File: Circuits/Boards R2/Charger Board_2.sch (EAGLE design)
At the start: 70 parts, among them CON1 ISP(2X3), CON10 HEADER_3X1, CON11 HEADER_3X1, CON12 HEADER_3X1, CON13 HEADER_4X1, CON2 SCREWTERMINAL_1X2, CON3 HEADER_3X1, CON4 HEADER_3X1, CON5 HEADER_3X1, CON6 HEADER_3X1, CON7 HEADER_3X1, CON8 HEADER_3X1, CON9 HEADER_3X1, IC1 NCP1117DT33G, T1 NPN2N2222, T2 NPN2N2222, T3 SI4421DY, U1 ATMEGA324P, U2 ACS711

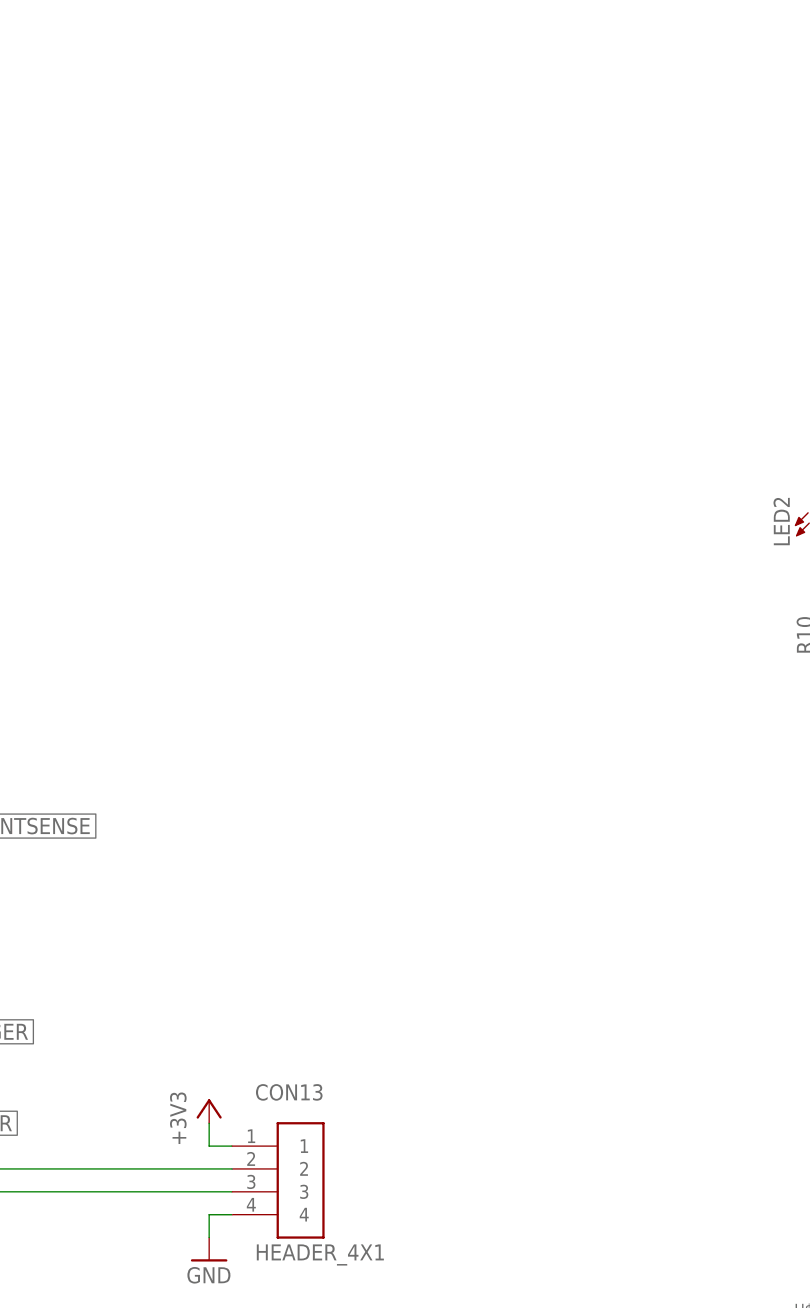
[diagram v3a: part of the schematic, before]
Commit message: 
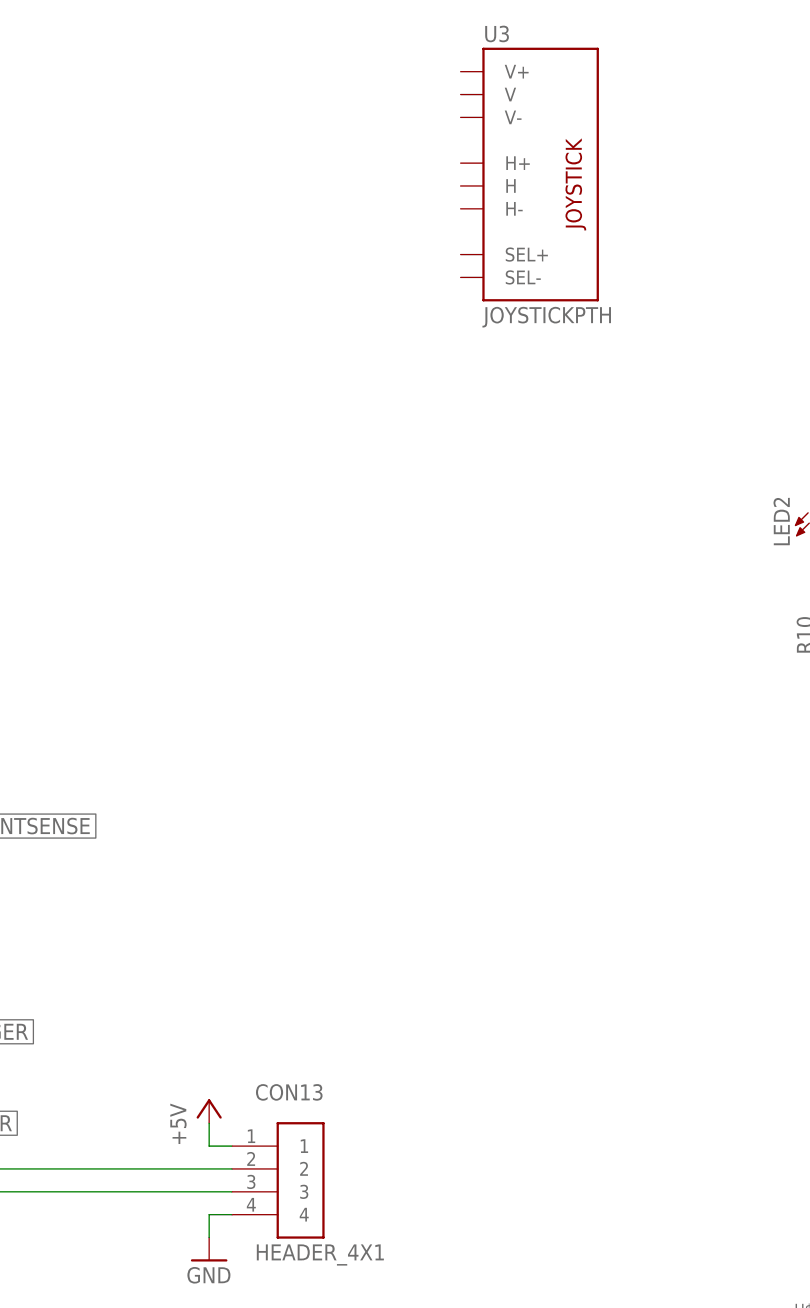
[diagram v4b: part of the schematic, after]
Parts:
- added U3: JOYSTICKPTH, SparkFun:JOYSTICKPTH
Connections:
- net +3V3: no longer CON13.1
- net +5V: now also CON13.1
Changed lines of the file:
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@@
 <layer number="51" name="tDocu" color="6" fill="1" visible="no" active="no"/>
 <layer number="52" name="bDocu" color="7" fill="1" visible="no" active="no"/>
+<layer number="53" name="tGND_GNDA" color="7" fill="9" visible="no" active="no"/>
+<layer number="54" name="bGND_GNDA" color="1" fill="9" visible="no" active="no"/>
+<layer number="56" name="wert" color="7" fill="1" visible="no" active="no"/>
 <layer number="91" name="Nets" color="2" fill="1" visible="yes" active="yes"/>
 <layer number="92" name="Busses" color="1" fill="1" visible="yes" active="yes"/>
@@
 <layer number="97" name="Info" color="7" fill="1" visible="yes" active="yes"/>
 <layer number="98" name="Guide" color="6" fill="1" visible="yes" active="yes"/>
+<layer number="100" name="Muster" color="7" fill="1" visible="no" active="no"/>
+<layer number="101" name="Patch_Top" color="12" fill="4" visible="no" active="yes"/>
+<layer number="102" name="Vscore" color="7" fill="1" visible="no" active="yes"/>
+<layer number="103" name="tMap" color="7" fill="1" visible="no" active="yes"/>
+<layer number="104" name="Name" color="16" fill="1" visible="no" active="yes"/>
+<layer number="105" name="tPlate" color="7" fill="1" visible="no" active="yes"/>
+<layer number="106" name="bPlate" color="7" fill="1" visible="no" active="yes"/>
+<layer number="107" name="Crop" color="7" fill="1" visible="no" active="yes"/>
+<layer number="116" name="Patch_BOT" color="9" fill="4" visible="no" active="yes"/>
+<layer number="121" name="_tsilk" color="7" fill="1" visible="no" active="yes"/>
+<layer number="122" name="_bsilk" color="7" fill="1" visible="no" active="yes"/>
+<layer number="125" name="_tNames" color="7" fill="1" visible="no" active="yes"/>
+<layer number="144" name="Drill_legend" color="7" fill="1" visible="no" active="yes"/>
+<layer number="151" name="HeatSink" color="7" fill="1" visible="no" active="yes"/>
 <layer number="200" name="200bmp" color="1" fill="10" visible="no" active="no"/>
+<layer number="201" name="201bmp" color="2" fill="10" visible="no" active="yes"/>
+<layer number="202" name="202bmp" color="3" fill="10" visible="no" active="yes"/>
+<layer number="203" name="203bmp" color="4" fill="10" visible="no" active="yes"/>
+<layer number="204" name="204bmp" color="5" fill="10" visible="no" active="yes"/>
+<layer number="205" name="205bmp" color="6" fill="10" visible="no" active="yes"/>
+<layer number="206" name="206bmp" color="7" fill="10" visible="no" active="yes"/>
+<layer number="207" name="207bmp" color="8" fill="10" visible="no" active="yes"/>
+<layer number="208" name="208bmp" color="9" fill="10" visible="no" active="yes"/>
+<layer number="209" name="209bmp" color="7" fill="1" visible="no" active="yes"/>
+<layer number="210" name="210bmp" color="7" fill="1" visible="no" active="yes"/>
+<layer number="211" name="211bmp" color="7" fill="1" visible="no" active="yes"/>
+<layer number="212" name="212bmp" color="7" fill="1" visible="no" active="yes"/>
+<layer number="213" name="213bmp" color="7" fill="1" visible="no" active="yes"/>
+<layer number="214" name="214bmp" color="7" fill="1" visible="no" active="yes"/>
+<layer number="215" name="215bmp" color="7" fill="1" visible="no" active="yes"/>
+<layer number="216" name="216bmp" color="7" fill="1" visible="no" active="yes"/>
+<layer number="217" name="217bmp" color="18" fill="1" visible="no" active="no"/>
+<layer number="218" name="218bmp" color="19" fill="1" visible="no" active="no"/>
+<layer number="219" name="219bmp" color="20" fill="1" visible="no" active="no"/>
+<layer number="220" name="220bmp" color="21" fill="1" visible="no" active="no"/>
+<layer number="221" name="221bmp" color="22" fill="1" visible="no" active="no"/>
+<layer number="222" name="222bmp" color="23" fill="1" visible="no" active="no"/>
+<layer number="223" name="223bmp" color="24" fill="1" visible="no" active="no"/>
+<layer number="224" name="224bmp" color="25" fill="1" visible="no" active="no"/>
+<layer number="250" name="Descript" color="3" fill="1" visible="no" active="no"/>
+<layer number="251" name="SMDround" color="12" fill="11" visible="no" active="no"/>
+<layer number="254" name="cooling" color="7" fill="1" visible="no" active="yes"/>
 </layers>
 <schematic xreflabel="%F%N/%S.%C%R" xrefpart="/%S.%C%R">
@@
 <part name="CON13" library="Mechanical" deviceset="HEADER_4X1" device=""/>
 <part name="GND11" library="Supply" deviceset="GND" device=""/>
-<part name="+3V8" library="Supply" deviceset="+3V3" device=""/>
+<part name="P+2" library="Supply" deviceset="+5V" device=""/>
+<part name="U3" library="SparkFun" deviceset="JOYSTICK" device="PTH"/>
 </parts>
 <sheets>
@@
 <instance part="CON13" gate="G$1" x="99.06" y="0"/>
 <instance part="GND11" gate="1" x="91.44" y="-10.16"/>
-<instance part="+3V8" gate="G$1" x="91.44" y="7.62"/>
+<instance part="P+2" gate="1" x="91.44" y="7.62"/>
+<instance part="U3" gate="G$1" x="129.54" y="111.76"/>
 </instances>
 <busses>
@@
 <pinref part="P+1" gate="1" pin="+5V"/>
 </segment>
+<segment>
+<pinref part="CON13" gate="G$1" pin="1"/>
+<wire x1="93.98" y1="2.54" x2="91.44" y2="2.54" width="0.1524" layer="91"/>
+<wire x1="91.44" y1="2.54" x2="91.44" y2="5.08" width="0.1524" layer="91"/>
+<pinref part="P+2" gate="1" pin="+5V"/>
+</segment>
 </net>
 <net name="CURRENTSENSE" class="0">
@@
 <pinref part="+3V4" gate="G$1" pin="+3V3"/>
 </segment>
-<segment>
-<pinref part="CON13" gate="G$1" pin="1"/>
-<wire x1="93.98" y1="2.54" x2="91.44" y2="2.54" width="0.1524" layer="91"/>
-<wire x1="91.44" y1="2.54" x2="91.44" y2="5.08" width="0.1524" layer="91"/>
-<pinref part="+3V8" gate="G$1" pin="+3V3"/>
-</segment>
-</net>
+</net>

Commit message: 
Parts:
- removed LED7: IR, Passive:LED5MMRA
- added C12, C13, C14, C9: .1uf, Passive:CAP0603
- added C8: 10uf, Passive:CAP0805
- added S1: (no value), switch-omron:10-XX
- R10, R11, R12, R13, R14: value (none) -> 18
- R15: value (none) -> 10k
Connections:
- net N$2 renamed MOSI
- net N$3 renamed MISO
- net N$5 renamed SCK
- removed net N$18: LED7.C, R15.2
- removed net N$6: CON1.!RESET, R7.2, U1.!RESET
- new net BUTTON: C13.1, R15.2, U1.PA3(ADC3/PCINT3), U3.SEL-
- new net HORIZONTAL: U1.PA2(ADC2/PCINT2), U3.H
- new net RESET: C14.1, CON1.!RESET, R7.2, S1.P, S1.P1, U1.!RESET
- new net VERTICAL: U1.PA1(ADC1/PCINT1), U3.V
- net +3V3: now also U3.H+, U3.SEL+, U3.V+; no longer C2.1, C6.1, C7.1, LED2.A, LED3.A, LED4.A, LED5.A, LED6.A, LED7.A
- net +5V: now also C12.1, C2.1, C6.1, C7.1, C8.1, C9.1, LED2.A, LED3.A, LED4.A, LED5.A, LED6.A
- net GND: now also C12.2, C13.2, C14.2, C8.2, C9.2, R15.1, S1.S, S1.S1, U3.H-, U3.V-
- net N$10: no longer R15.1
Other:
- moved on the sheet: B1, C2, C7, CON1, LED1, LED2, LED3, LED4, LED5, LED6, R1, R10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

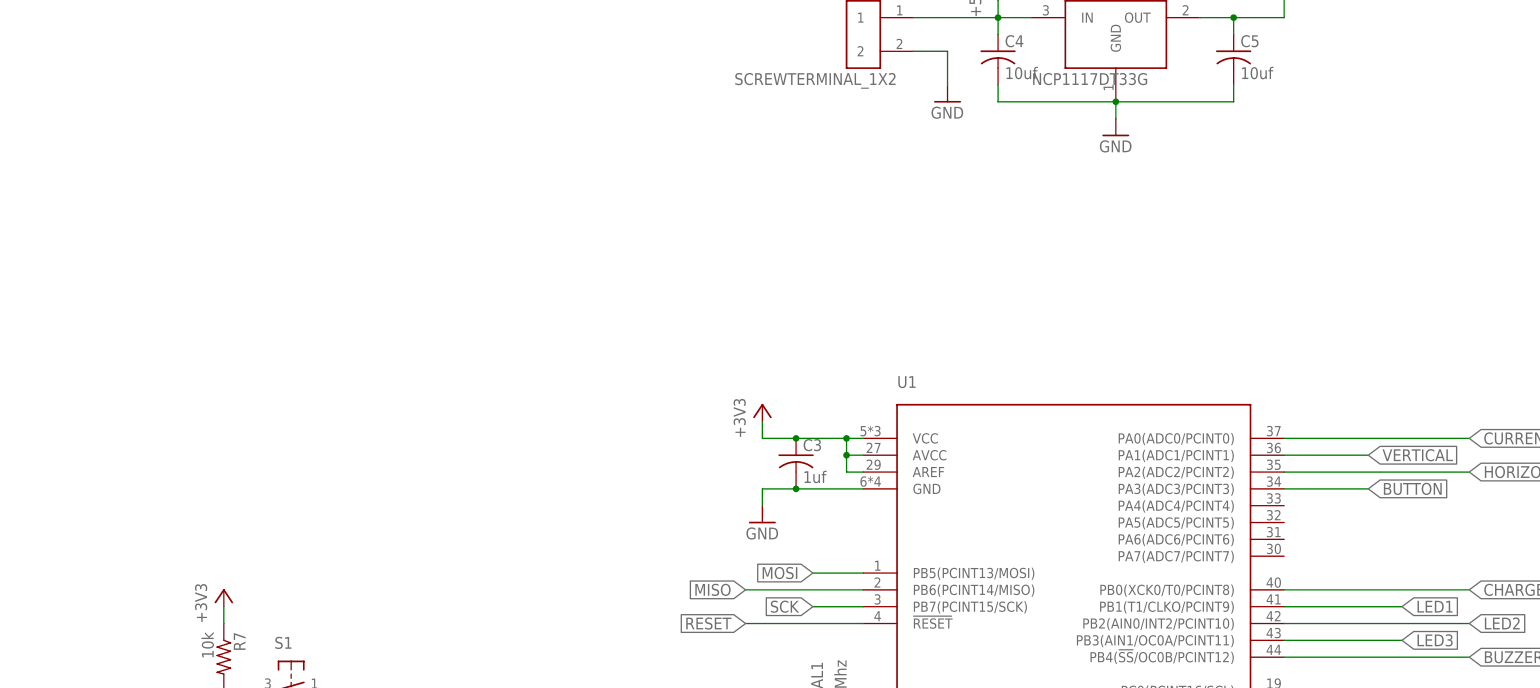
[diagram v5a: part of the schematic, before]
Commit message: 
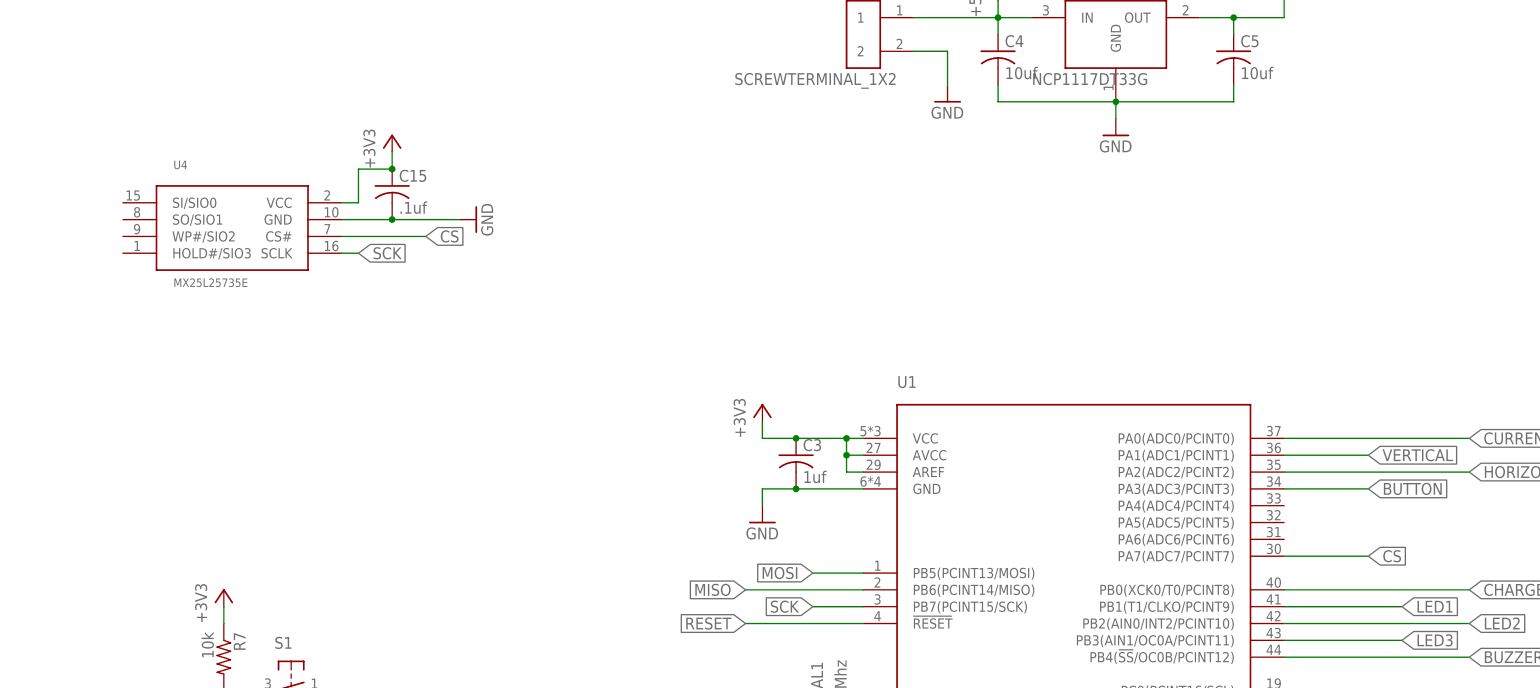
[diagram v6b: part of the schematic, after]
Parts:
- added C15: .1uf, Passive:CAP0603
- added U4: MX25L25735E, DigitalIC:MX25L25735E
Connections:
- new net CS: U1.PA7(ADC7/PCINT7), U4.CS#
- net +3V3: now also C15.1, U4.VCC
- net GND: now also C15.2, U4.GND
- net SCK: now also U4.SCLK
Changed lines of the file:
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@@
 <part name="GND16" library="Supply" deviceset="GND" device=""/>
 <part name="C14" library="Passive" deviceset="CAP" device="0603" value=".1uf"/>
+<part name="U4" library="DigitalIC" deviceset="MX25L25735E" device=""/>
+<part name="C15" library="Passive" deviceset="CAP" device="0603" value=".1uf"/>
+<part name="+3V1" library="Supply" deviceset="+3V3" device=""/>
+<part name="GND17" library="Supply" deviceset="GND" device=""/>
 </parts>
 <sheets>
@@
 <instance part="GND16" gate="1" x="-106.68" y="-2.54" rot="R90"/>
 <instance part="C14" gate="G$1" x="-119.38" y="-7.62" rot="R90"/>
+<instance part="U4" gate="G$1" x="-127" y="68.58"/>
+<instance part="C15" gate="G$1" x="-104.14" y="73.66"/>
+<instance part="+3V1" gate="G$1" x="-104.14" y="83.82"/>
+<instance part="GND17" gate="1" x="-91.44" y="71.12" rot="R90"/>
 </instances>
 <busses>
@@
 <wire x1="-111.76" y1="-2.54" x2="-111.76" y2="-7.62" width="0.1524" layer="91"/>
 <wire x1="-111.76" y1="-7.62" x2="-116.84" y2="-7.62" width="0.1524" layer="91"/>
+</segment>
+<segment>
+<pinref part="U4" gate="G$1" pin="GND"/>
+<pinref part="C15" gate="G$1" pin="2"/>
+<wire x1="-111.76" y1="71.12" x2="-104.14" y2="71.12" width="0.1524" layer="91"/>
+<wire x1="-104.14" y1="71.12" x2="-93.98" y2="71.12" width="0.1524" layer="91"/>
+<junction x="-104.14" y="71.12"/>
+<pinref part="GND17" gate="1" pin="GND"/>
 </segment>
 </net>
@@
 <wire x1="114.3" y1="101.6" x2="119.38" y2="101.6" width="0.1524" layer="91"/>
 </segment>
+<segment>
+<pinref part="U4" gate="G$1" pin="VCC"/>
+<wire x1="-111.76" y1="73.66" x2="-109.22" y2="73.66" width="0.1524" layer="91"/>
+<wire x1="-109.22" y1="73.66" x2="-109.22" y2="78.74" width="0.1524" layer="91"/>
+<pinref part="C15" gate="G$1" pin="1"/>
+<wire x1="-109.22" y1="78.74" x2="-104.14" y2="78.74" width="0.1524" layer="91"/>
+<wire x1="-104.14" y1="78.74" x2="-104.14" y2="81.28" width="0.1524" layer="91"/>
+<pinref part="+3V1" gate="G$1" pin="+3V3"/>
+<junction x="-104.14" y="78.74"/>
+</segment>
 </net>
 <net name="SECTION2" class="0">
@@
 <label x="-40.64" y="12.7" size="1.778" layer="91" rot="R180" xref="yes"/>
 </segment>
-</net>
+<segment>
+<pinref part="U4" gate="G$1" pin="SCLK"/>
+<wire x1="-111.76" y1="66.04" x2="-109.22" y2="66.04" width="0.1524" layer="91"/>
+<label x="-109.22" y="66.04" size="1.778" layer="91" xref="yes"/>
+</segment>
+</net>
+<net name="CS" class="0">
+<segment>
+<pinref part="U4" gate="G$1" pin="CS#"/>
+<wire x1="-111.76" y1="68.58" x2="-99.06" y2="68.58" width="0.1524" layer="91"/>
+<label x="-99.06" y="68.58" size="1.778" layer="91" xref="yes"/>
+</segment>
+<segment>
+<pinref part="U1" gate="G$1" pin="PA7(ADC7/PCINT7)"/>
+<wire x1="30.48" y1="20.32" x2="43.18" y2="20.32" width="0.1524" layer="91"/>
+<label x="43.18" y="20.32" size="1.778" layer="91" xref="yes"/>
+</segment>
+</net>
